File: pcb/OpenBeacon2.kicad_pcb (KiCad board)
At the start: 4 copper layers, 120 x 100 mm, 262 parts, among them J1 Bias V, J10 UART, J11 BNC, J12 USB_C_Receptacle, J13 UPDI, J14 PPS, J15 U.FL, J16 SMA CLKIN, J2 PAI+, J3 PAI-, J4 Digital IO, J5 ADC Inputs, J6 SMA, J8 I2C Bus, J9 GND, K1 G6K-2F-Y-DC5, K2 G6K-2F-Y-DC5, K3 G6K-2F-Y-DC5, K4 G6K-2F-Y-DC5, K5 G6K-2F-Y-DC5, K6 G6K-2F-Y-DC5, Q1 2N7002, Q2 MMBT4403, Q3 BS170, Q4 2N7002, Q5 2N7002, Q6 AO3400A, Q7 AO3400A, Q8 BS170, U1 TLV61046A, U10 CP2102N-A02-GQFN24, U11 TLV75533PDBV, U12 MAX-M10S-00B, U13 TPS22941, U2 25.000 MHz TCXO, U3 SN74LVC1G17, U4 SI5351C-B-GMR, U5 MCP4725A1T-E/CH, U8 24AA64T, U9 AVR128DA48-E/PT, Y1 32.768kHz

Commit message: PCB Rev C: J11 BNC rotated 180 (faces back edge), L2 left for 1.2mm Q3 clearance, 38 silk leader lines; 3D models for J11/J6/J16/J12/L1/L2/U2/U4/U12/DS1/toroids, fix SOT23 model scale
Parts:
- moved C34 87.5 mm to (103.8, 158.0), turned to 0 degrees
- moved C30 86.6 mm to (174.1, 106.5)
- moved C33 33.1 mm to (104.3, 155.1)
- moved C36 32.3 mm to (142.1, 164.1)
- moved C32 30.1 mm to (136.0, 155.2)
- moved C40 28.1 mm to (113.3, 162.3)
- moved C38 19.9 mm to (138.1, 164.7), turned to 90 degrees
- moved J11 14.2 mm to (199.5, 100.0), turned to 180 degrees
- moved R7 12.9 mm to (106.2, 138.3), turned to 0 degrees
- moved D18 12.8 mm to (103.2, 142.9)
- moved D9 9.70 mm to (104.2, 151.5)
- moved J1 6.39 mm to (106.8, 141.4)
- moved C31 5.34 mm to (110.8, 159.5), turned to 0 degrees
- moved C9 4.53 mm to (103.2, 146.6), turned to 90 degrees
- moved C39 3.66 mm to (118.3, 163.1), turned to 0 degrees
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
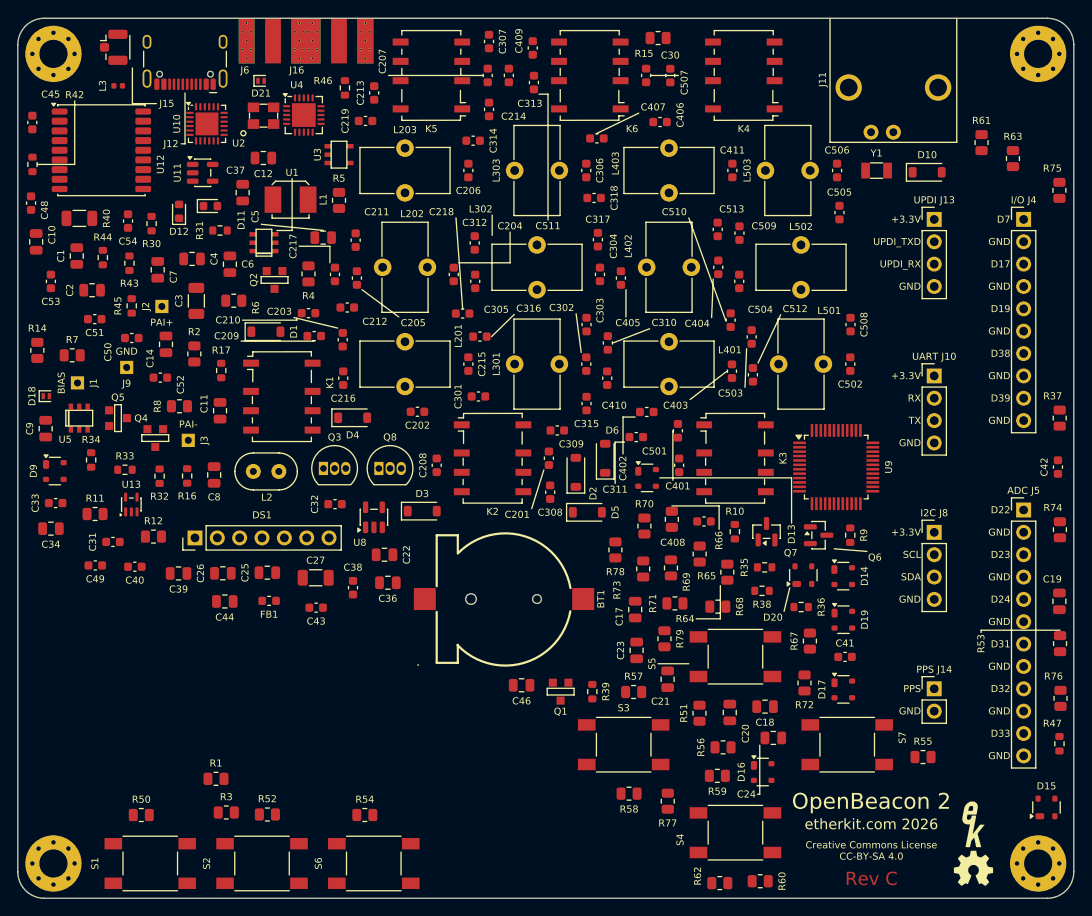
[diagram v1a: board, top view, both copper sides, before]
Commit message: PCB Rev C: SMA J6/J16 spread to 16 mm c-c (15 mm from USB-C), J12 USB-C left, GPS U.FL J15 to left edge beside U12, synth U2/U4/U3 re-centred behind SMAs, toroid pitch 14 mm, K3 left for U9 clearance; gate.py passes
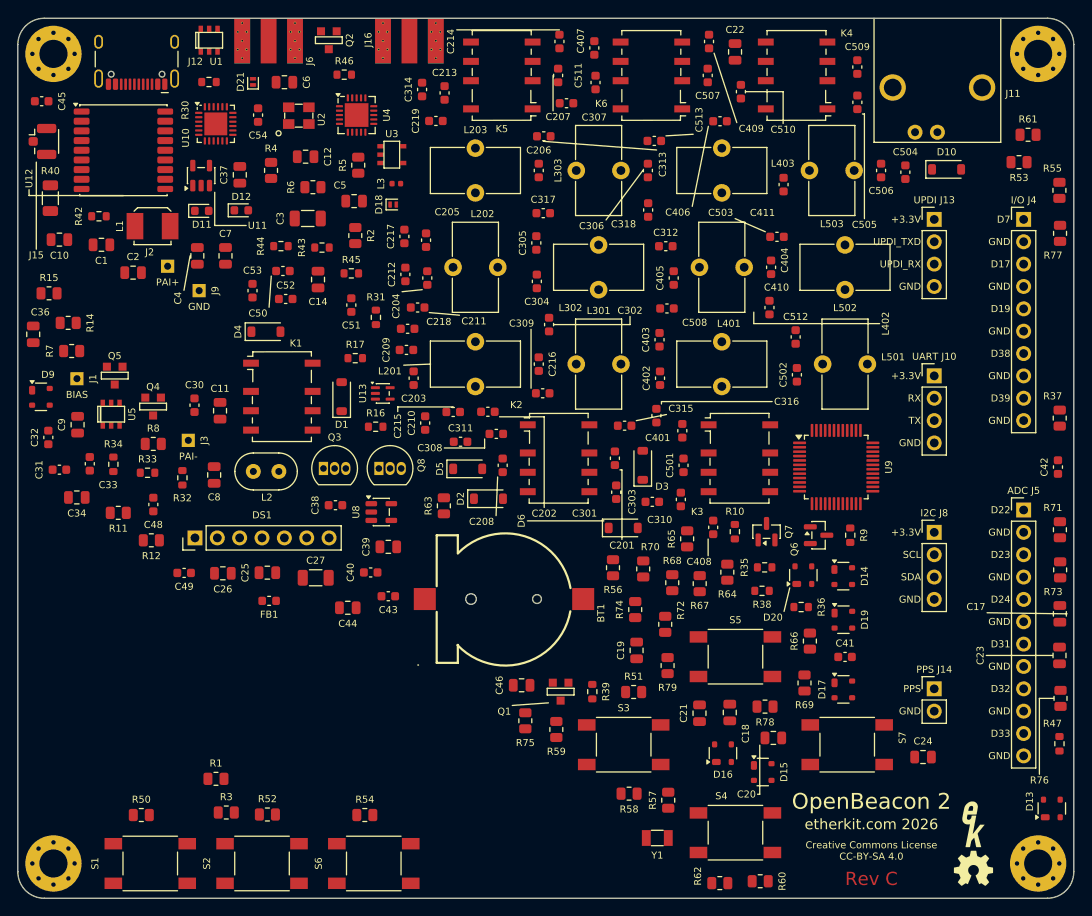
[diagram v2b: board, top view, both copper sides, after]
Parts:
- moved R75 85.5 mm to (157.7, 179.8)
- moved Y1 79.8 mm to (172.7, 193.2)
- moved R77 78.4 mm to (218.4, 124.4)
- moved R63 75.8 mm to (148.4, 155.4)
- moved R15 75.0 mm to (103.5, 131.3)
- moved C22 69.7 mm to (181.5, 103.8), turned to 90 degrees
- moved R55 66.2 mm to (218.4, 119.6), turned to 90 degrees
- moved C30 65.8 mm to (120.1, 144.0)
- moved D13 59.4 mm to (217.5, 189.8), turned to 90 degrees
- moved R53 54.9 mm to (213.8, 116.4), turned to 0 degrees
- moved C36 49.2 mm to (101.8, 135.9), turned to 90 degrees
- moved R74 49.1 mm to (170.2, 167.2)
- moved C19 48.4 mm to (170.3, 171.8)
- moved C17 48.3 mm to (218.4, 167.7)
- moved C23 48.1 mm to (218.4, 172.4)
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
